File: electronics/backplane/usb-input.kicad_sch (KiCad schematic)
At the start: 5 parts, among them J1 USB_C_SOCKET_RA_PTH_SIMPLE, U1 USBLC6

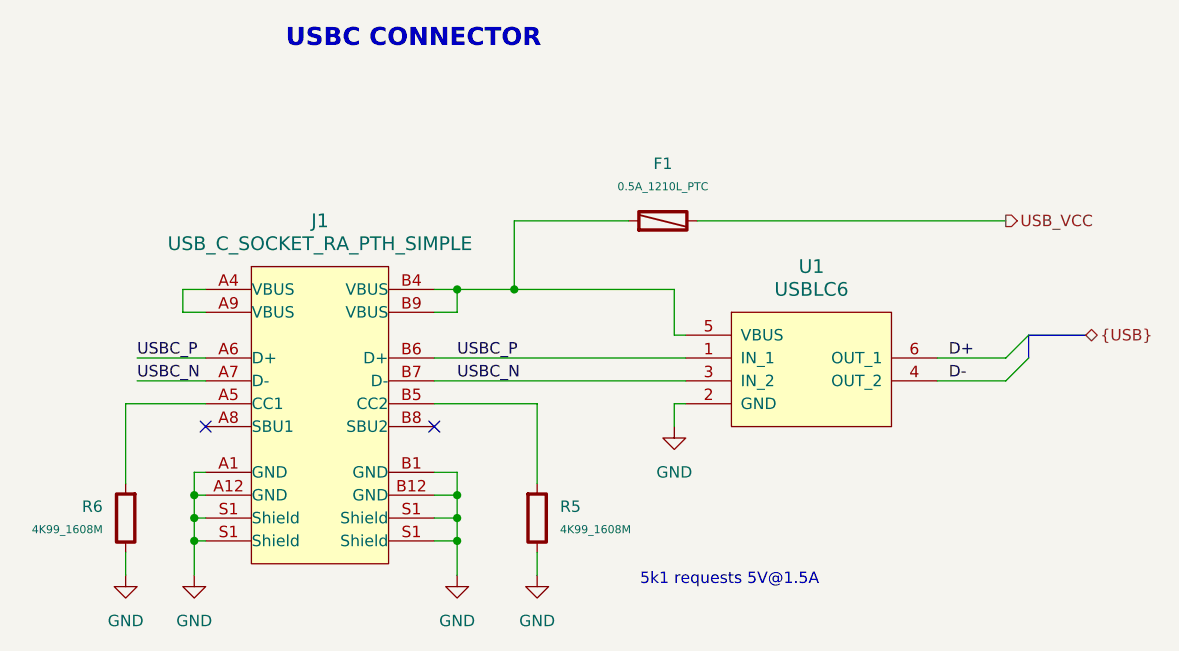
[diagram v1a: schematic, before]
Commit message: Continue backplane design Cleanup schematic, most routing and placement done
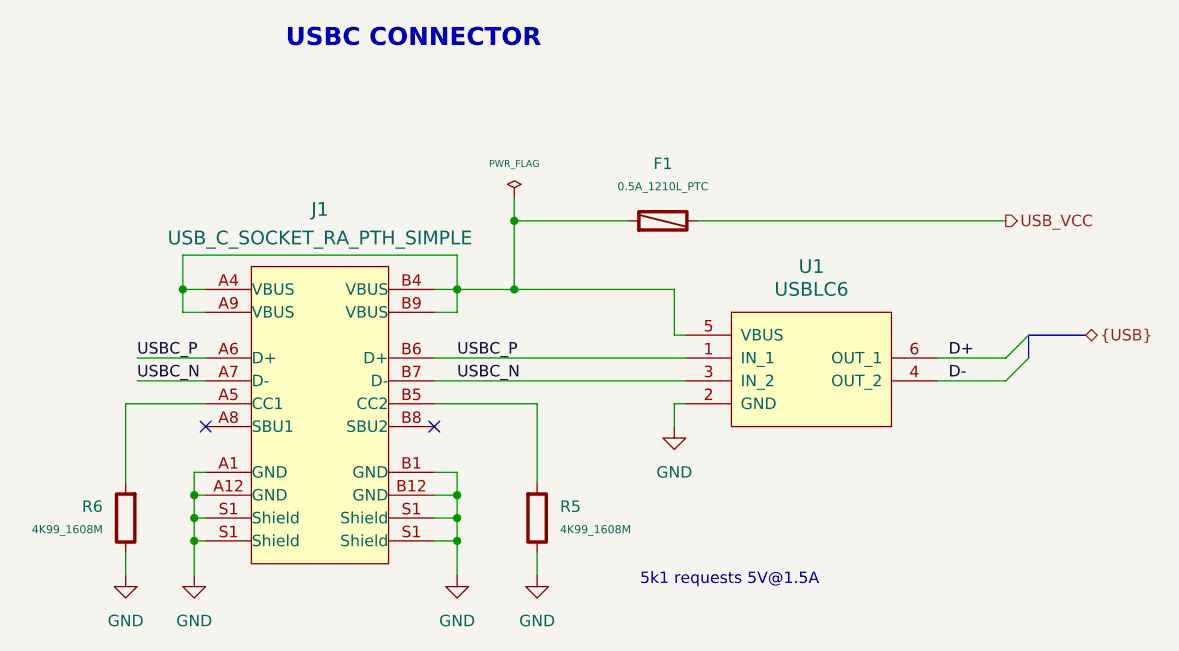
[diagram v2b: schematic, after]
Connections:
- net at F1.1, J1.B4 (VBUS), J1.B9 (VBUS)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: now also J1.A4 (VBUS), J1.A9 (VBUS)
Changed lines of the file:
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@@
   (junction (at 139.7 99.06) (diameter 0) (color 0 0 0 0)
+  )
+  (junction (at 146.05 68.58) (diameter 0) (color 0 0 0 0)
+  )
+  (junction (at 109.22 76.2) (diameter 0) (color 0 0 0 0)
   )
   (junction (at 139.7 76.2) (diameter 0) (color 0 0 0 0)
@@
     (stroke (width 0) (type default))
   )
+  (wire (pts (xy 146.05 66.04) (xy 146.05 68.58))
+    (stroke (width 0) (type default))
+  )
   (wire (pts (xy 137.16 78.74) (xy 139.7 78.74))
     (stroke (width 0) (type default))
@@
     (stroke (width 0) (type default))
   )
+  (wire (pts (xy 109.22 72.39) (xy 109.22 76.2))
+    (stroke (width 0) (type default))
+  )
+  (wire (pts (xy 139.7 72.39) (xy 109.22 72.39))
+    (stroke (width 0) (type default))
+  )
   (wire (pts (xy 137.16 101.6) (xy 139.7 101.6))
     (stroke (width 0) (type default))
@@
   )
   (wire (pts (xy 139.7 101.6) (xy 139.7 104.14))
+    (stroke (width 0) (type default))
+  )
+  (wire (pts (xy 139.7 76.2) (xy 139.7 72.39))
     (stroke (width 0) (type default))
   )
@@
   )
   (symbol (lib_id "appli_usb:USB_C_SOCKET_RA_PTH_SIMPLE") (at 124.46 91.44 0) (unit 1)
-    (in_bom yes) (on_board yes) (dnp no) (fields_autoplaced)
-    (property "Reference" "J1" (at 124.46 68.58 0)
+    (in_bom yes) (on_board yes) (dnp no)
+    (property "Reference" "J1" (at 124.46 67.31 0)
       (effects (font (size 1.524 1.524)))
     )
-    (property "Value" "USB_C_SOCKET_RA_PTH_SIMPLE" (at 124.46 71.12 0)
+    (property "Value" "USB_C_SOCKET_RA_PTH_SIMPLE" (at 124.46 70.485 0)
       (effects (font (size 1.524 1.524)))
     )
@@
         )
       )
+    )
+  )
+  (symbol (lib_id "appli_power:PWR_FLAG") (at 146.05 66.04 0) (unit 1)
+    (in_bom yes) (on_board yes) (dnp no) (fields_autoplaced)
+    (property "Reference" "#FLG02" (at 146.05 64.77 0)
+      (effects (font (size 0.762 0.762)) hide)
+    )
+    (property "Value" "PWR_FLAG" (at 146.05 62.23 0)
+      (effects (font (size 0.762 0.762)))
+    )
+    (property "Footprint" "" (at 146.05 66.04 0)
+      (effects (font (size 1.524 1.524)))
+    )
+    (property "Datasheet" "" (at 146.05 66.04 0)
+      (effects (font (size 1.524 1.524)))
+    )
+    (pin "1")
+    (instances
+      (project "backplane"
+        (path "/0bfdf1e4-b99d-46d4-adfc-42d352d37946/a8872965-354f-420e-ad8f-791e8338578a"
+          (reference "#FLG02") (unit 1)
+        )
+      )

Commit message: Backplane routing complete General schematic cleanup, board cosmetics etc
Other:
- title: (none) -> USB CONNECTION
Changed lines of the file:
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@@
 (kicad_sch (version 20230121) (generator eeschema)
   (paper "A4")
+  (title_block
+    (title "USB CONNECTION")
+    (date "2023-08-09")
+    (rev "V1.0")
+  )
   (junction (at 110.49 104.14) (diameter 0) (color 0 0 0 0)
   )

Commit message: Fixed backplane i2c connector 3D model/footprint linkage Also minor schematic cleanup
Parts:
- F1: manf# 1210L050YR -> 1210L050YR
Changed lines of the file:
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@@
       (effects (font (size 0.508 0.508)) hide)
     )
-    (property "manf#" " 1210L050YR" (at 162.56 63.246 90)
+    (property "manf#" "1210L050YR" (at 162.56 63.246 90)
       (effects (font (size 0.508 0.508)) hide)
     )
